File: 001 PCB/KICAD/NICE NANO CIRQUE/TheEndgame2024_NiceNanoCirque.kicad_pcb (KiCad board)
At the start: 2 copper layers, 239 x 96.1 mm, 99 parts, among them J1 BATTERY_WIRES, J2 Cirque FFC 12P 0.5mm, SW10 SW_Push, SW11 SW_Push, SW12 SW_Push, SW13 SW_Push, SW14 SW_Push, SW15 SW_Push, SW16 SW_Push, SW17 SW_Push, SW18 SW_Push, SW19 SW_Push, SW2 SW_Push, SW20 SW_Push, SW21 SW_Push, SW22 SW_Push, SW23 SW_Push, SW24 SW_Push, SW25 SW_Push, SW26 SW_Push, SW27 SW_Push, SW28 SW_Push, SW29 SW_Push, SW3 SW_Push, SW30 SW_Push, SW31 SW_Push, SW32 SW_Push, SW33 SW_Push, SW34 SW_Push, SW35 SW_Push, SW36 SW_Push, SW37 SW_Push, SW38 PCM12SMTR, SW4 SW_Push, SW5 SW_Push, SW6 SW_Push, SW7 SW_Push, SW8 SW_Push, SW9 SW_Push, U2 nice!nano_v2

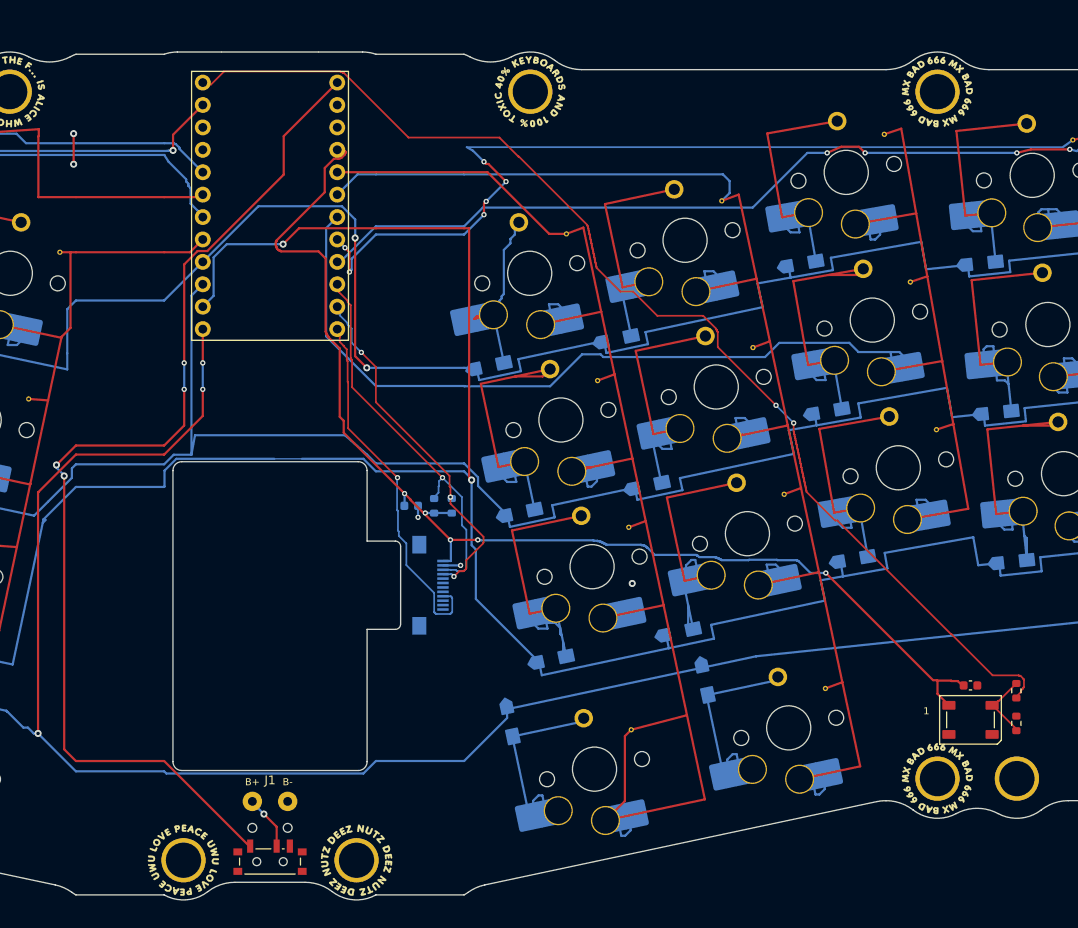
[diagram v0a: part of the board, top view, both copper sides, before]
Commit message: Move LED passives and power switch to the Cirque PCB underside
C1/R1/R2 sit under the LED so its case pocket shrinks to the LED itself.
SW38 moves under the nice!nano at the back edge with its slider through
the existing USB opening, removing the case's front switch channel. The
battery path is re-routed (0.4 mm); DRC stays clean. Previews now use the
board's stackup colours.

Co-Authored-By: Claude Opus 5.5 <noreply@anthropic.com>
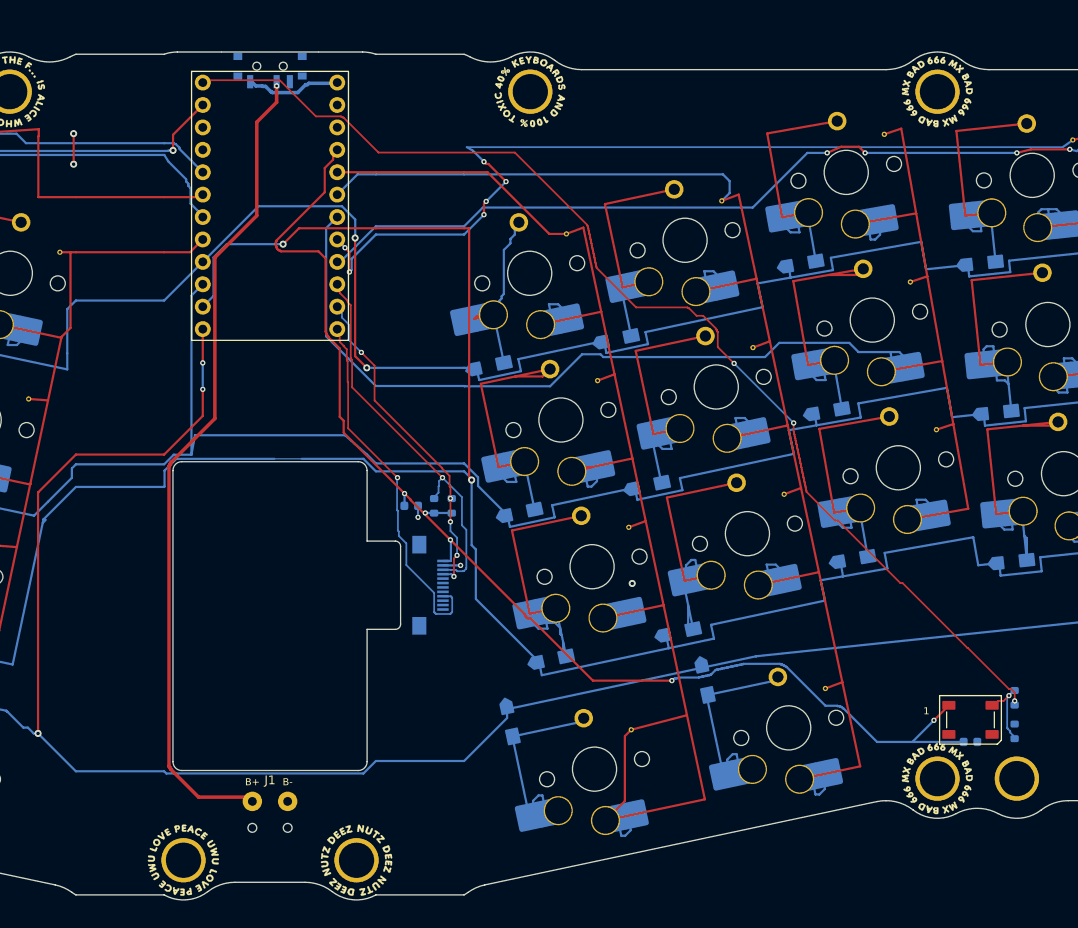
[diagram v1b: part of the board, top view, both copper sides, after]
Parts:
- C1, R1, R2, SW38: moved to B.Cu
- moved SW38 89.5 mm to (150.0, 64.5)
- moved C1 6.40 mm to (229.4, 140.8)
- moved R2 0.92 mm to (234.4, 139.6)
- moved R1 0.82 mm to (234.4, 135.8)
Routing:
- net VBAT_SW: track 121.2 -> 10.8 mm, vias 4 -> 0
- net VBAT: track 6.21 -> 93.8 mm
- net VCC_SW: track 135.7 -> 140.9 mm
- net SCL: track 40.6 -> 37.7 mm, vias 3 -> 5
- net LED_DATA: track 131.7 -> 129.2 mm, vias 2 -> 3
- net LED_DIN: track 7.61 -> 8.40 mm, vias 0 -> 1
